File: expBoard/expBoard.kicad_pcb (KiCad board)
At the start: 2 copper layers, 140 x 70 mm, 69 parts, among them P1 CONN_01X06, P2 CONN_01X04, P3 CONN_01X04, P4 DIL14, P5 CONN_01X06, P6 CONN_01X05, P7 DIL14, SW1 SWITCH_INV, SW2 SWITCH_INV, SW3 SWITCH_INV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

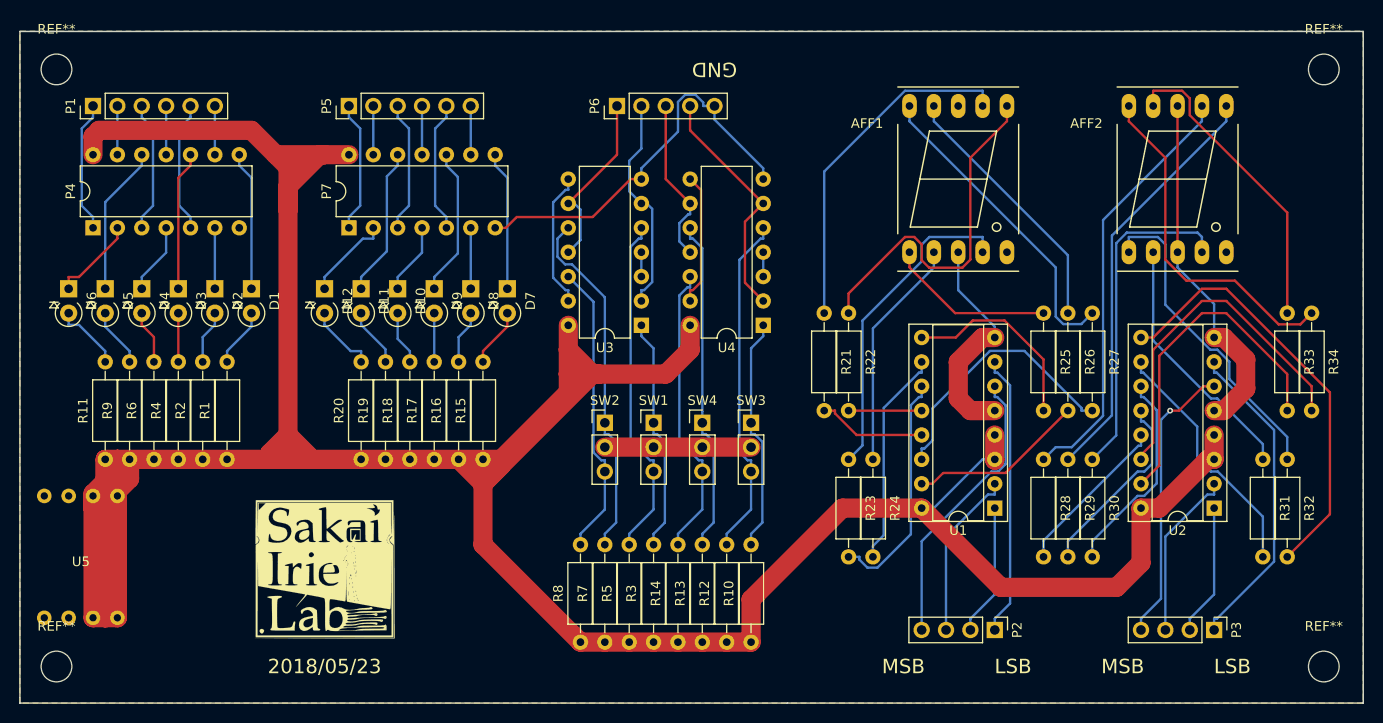
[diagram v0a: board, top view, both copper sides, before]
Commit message: Fix PCB layout of expBoard
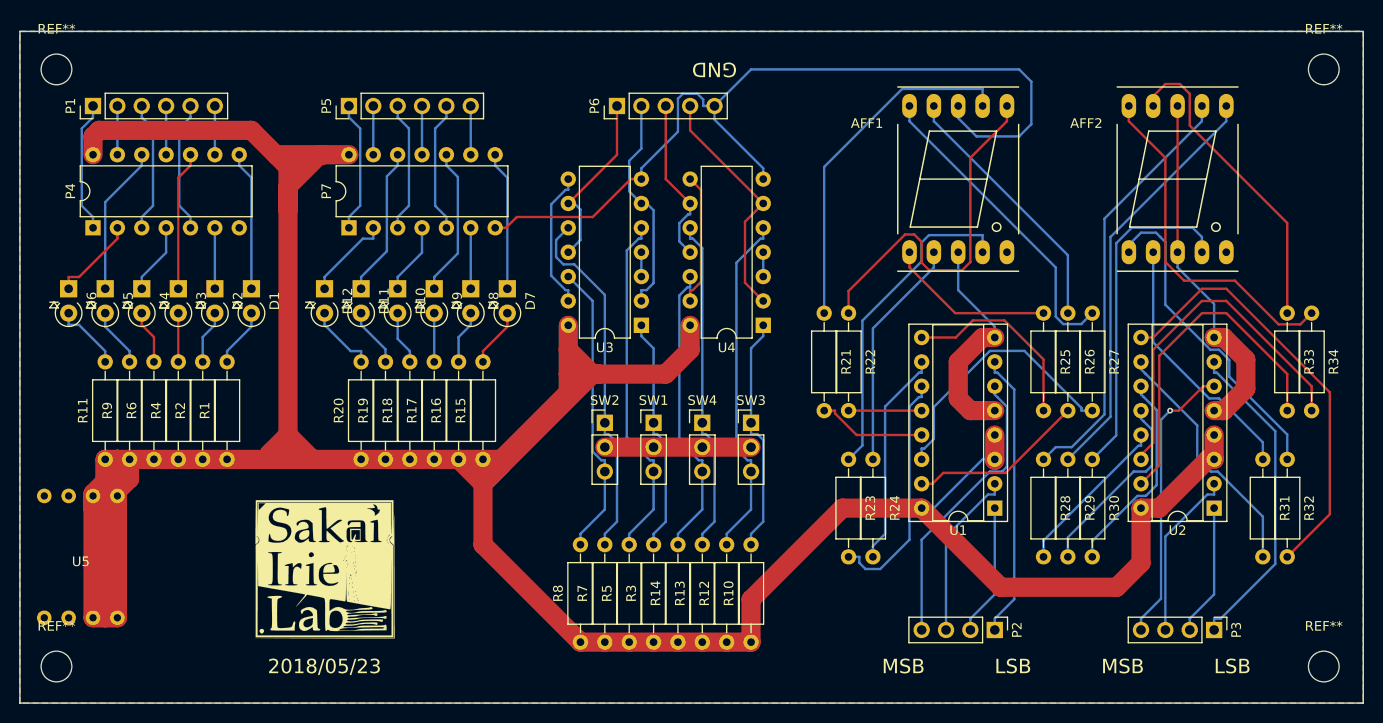
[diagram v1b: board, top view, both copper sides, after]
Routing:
- net GND: track 117.5 -> 167.7 mm
- net /oa1_LED: track 37.4 -> 38.4 mm
- net /oa2: track 24.6 -> 25.2 mm
- net /oa0_LED: track 36.3 -> 36.9 mm
- net /ob5_LED: track 32.3 -> 32.8 mm
